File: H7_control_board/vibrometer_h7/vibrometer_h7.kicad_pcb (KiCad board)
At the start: 4 copper layers, 100 x 130 mm, 73 parts, among them J1 USB_C_Receptacle_USB2.0_16P, J2 PJ-3270, Q201 BSS138, Q202 BSS138, SW201 SW_Push, SW501 SW_Push, SW502 SW_Push, U1 STM32H723VGTx, U2 USBLC6-2SC6, U3 AMS1117-3V3, U4 MT9700, U6 TPA6111A2

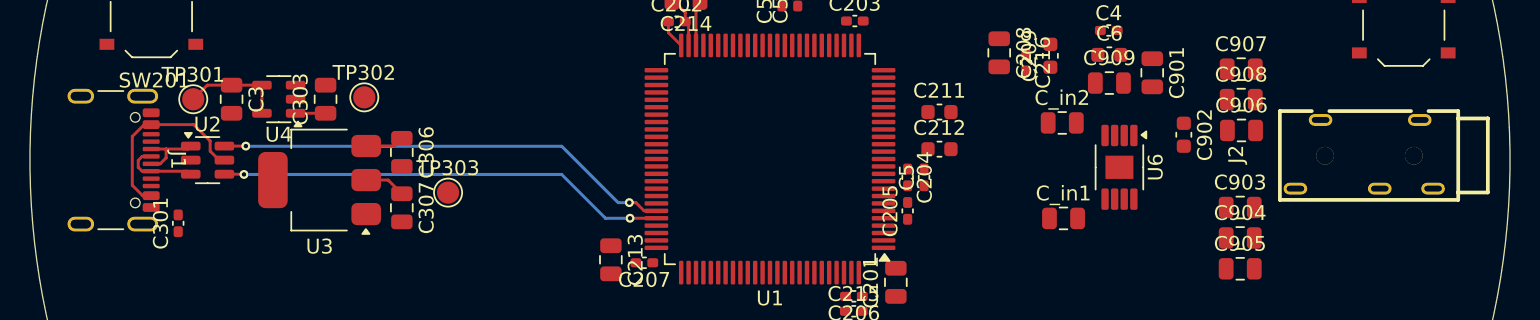
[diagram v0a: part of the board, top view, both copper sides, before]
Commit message: part selection for audio, schematic cleanup
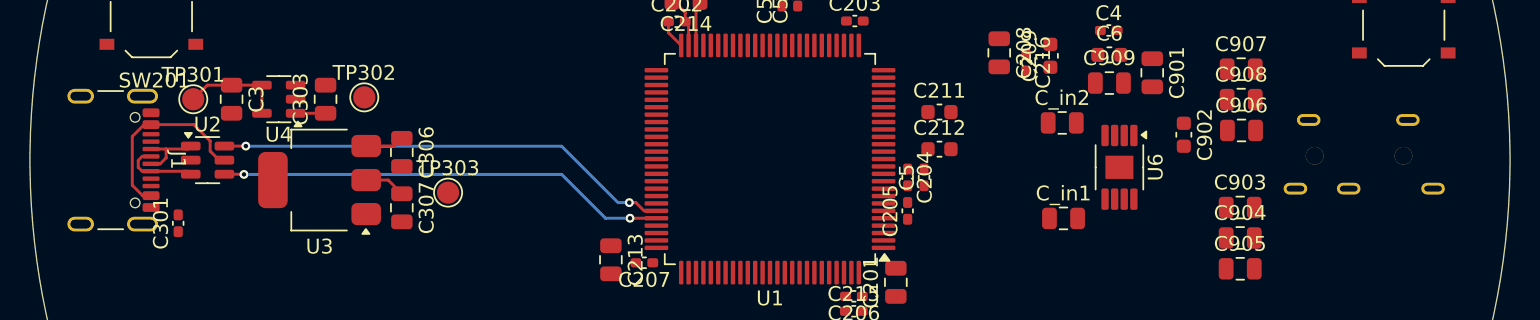
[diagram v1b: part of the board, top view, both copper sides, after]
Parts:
- J2: moved to B.Cu

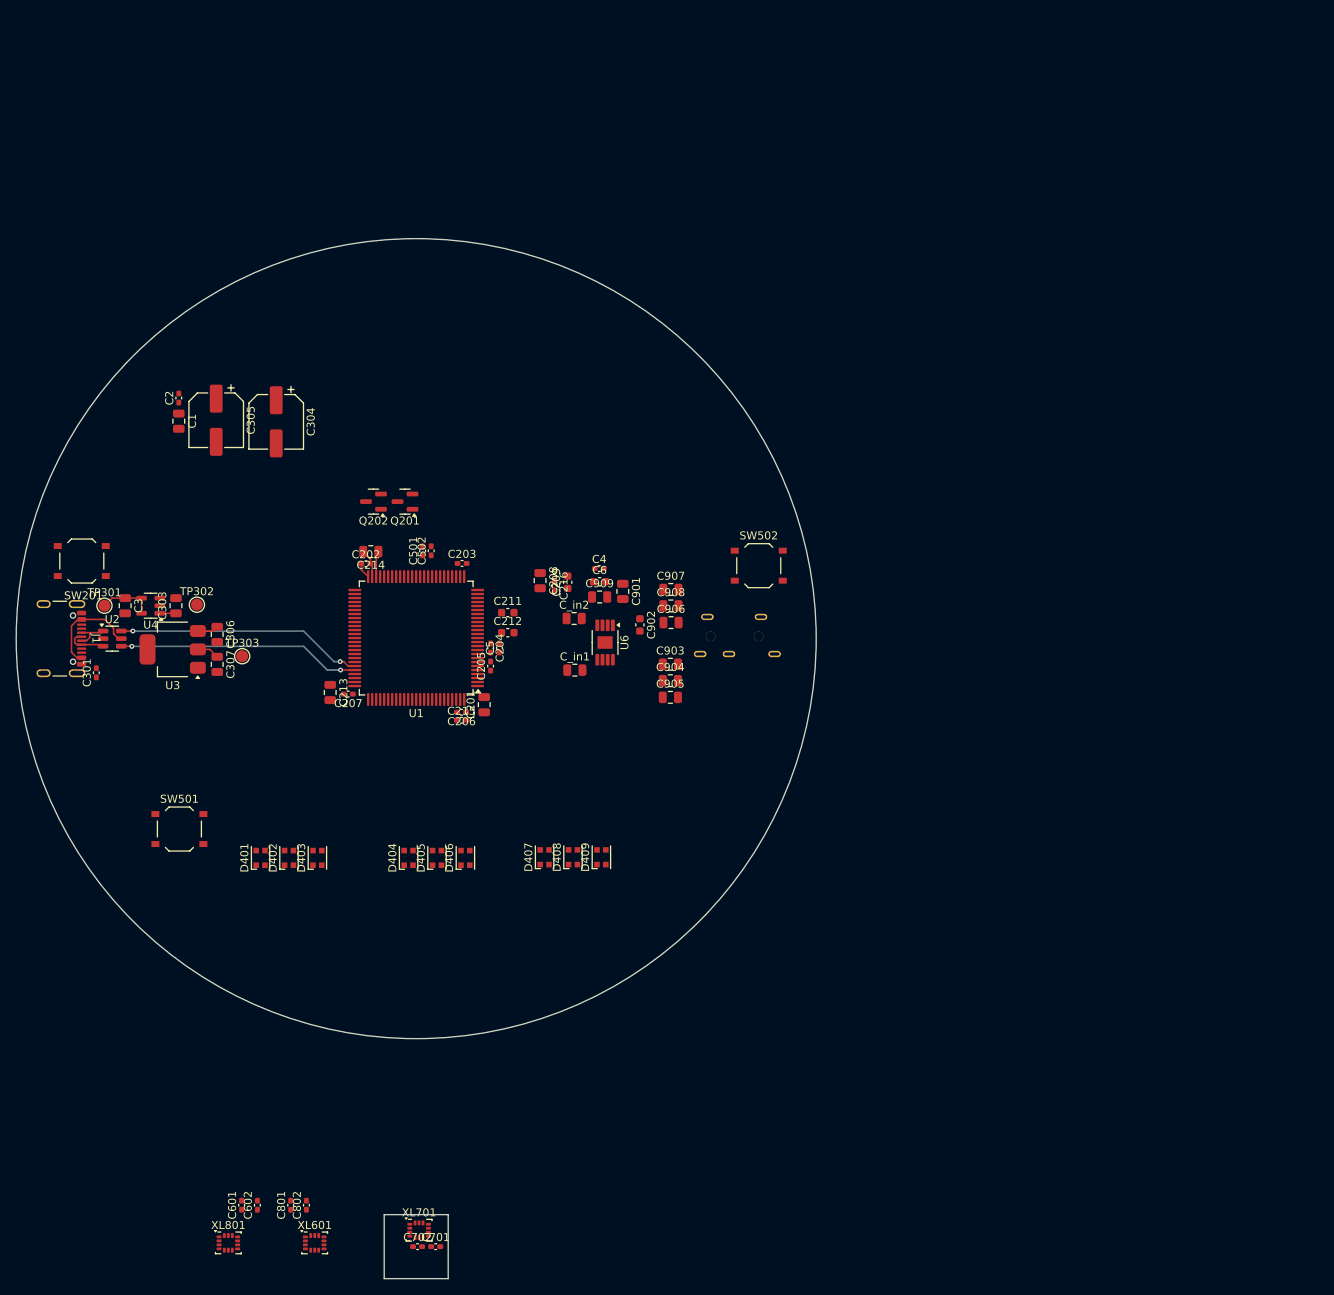
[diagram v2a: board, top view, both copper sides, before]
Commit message: first pass at board routing
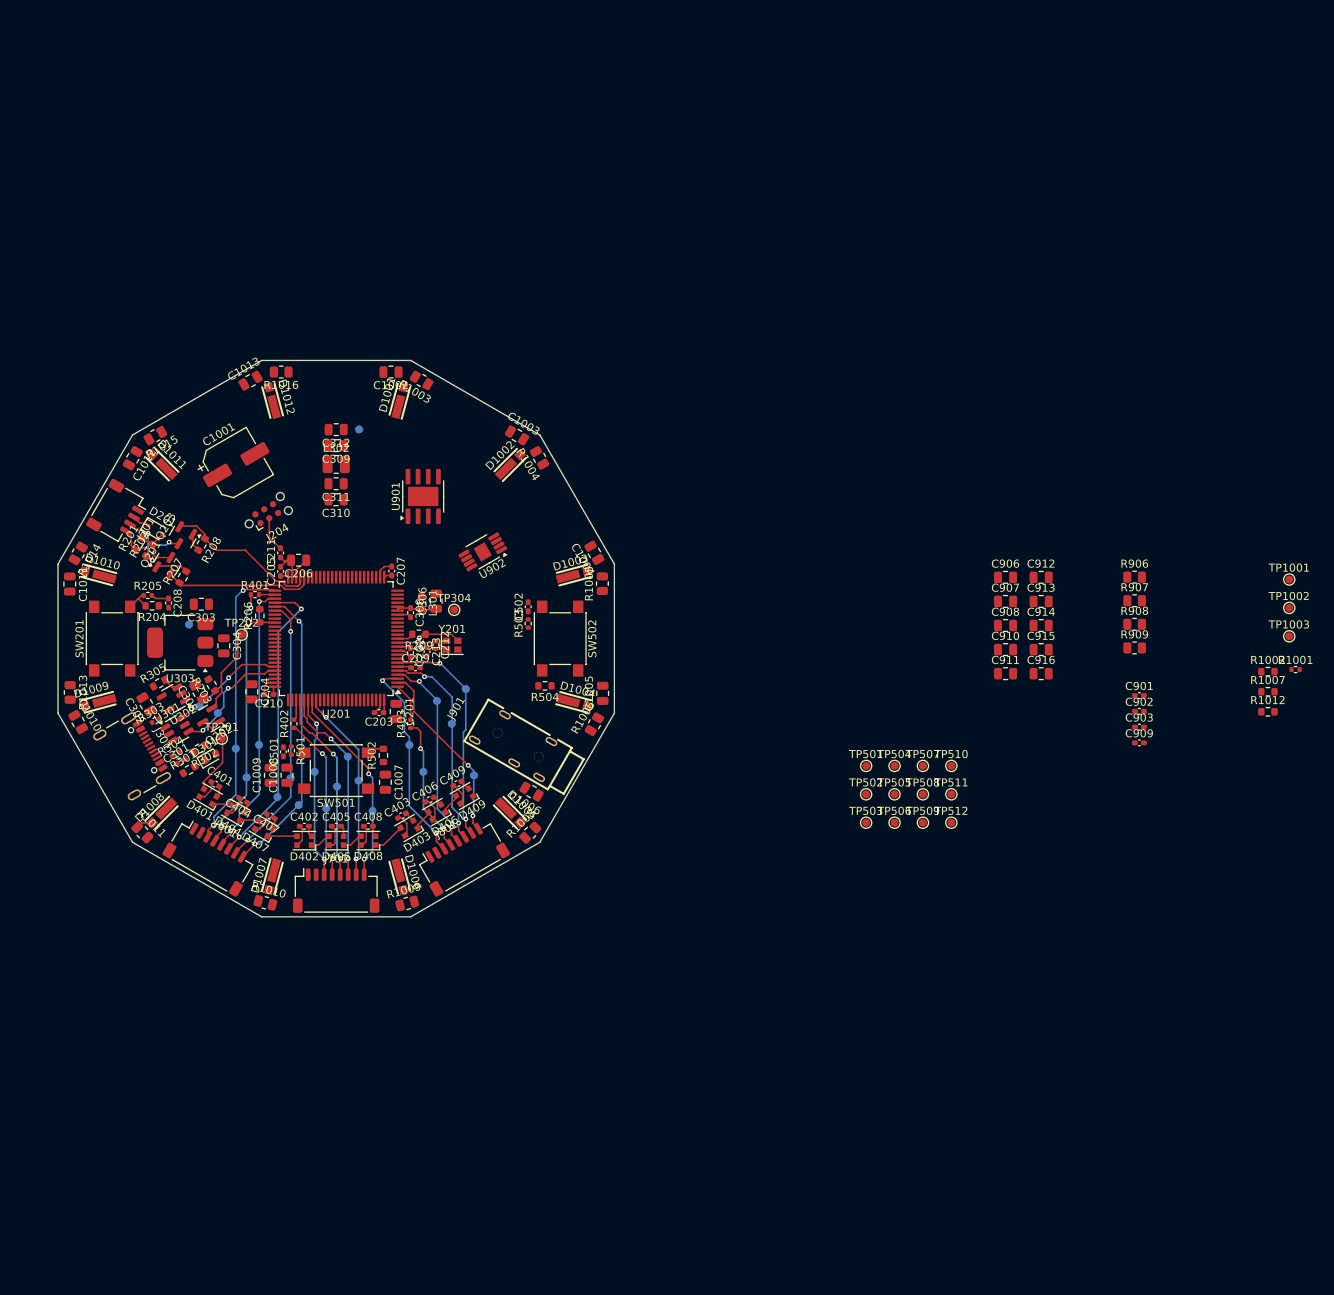
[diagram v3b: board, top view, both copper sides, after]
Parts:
- removed C1, C3: 10u, Capacitor_SMD:C_0805_2012Metric
- removed C2, C215, C216, C4, C5, C601, C602, C701, C702, C801, C802: 100n, Capacitor_SMD:C_0402_1005Metric_Pad0.74x0.62mm_HandSolder
- removed C214, C_in1, C_in2: 2u2, Capacitor_SMD:C_0805_2012Metric
- removed C307, C904, C905: 22u, Capacitor_SMD:C_0805_2012Metric
- removed C6: C_Small, Capacitor_SMD:C_0603_1608Metric
- removed J1: USB_C_Receptacle_USB2.0_16P, Connector_USB:USB_C_Receptacle_GCT_USB4105-xx-A_16P_TopMnt_Horizontal
- removed J2: PJ-3270, footprints:AUDIO-TH_PJ-3270
- removed TP301: TP_V_USB, TestPoint:TestPoint_Pad_D1.5mm
- removed TP303: TP_3V3, TestPoint:TestPoint_Pad_D1.5mm
- removed U1: STM32H723VGTx, Package_QFP:LQFP-100_14x14mm_P0.5mm
- removed U2: USBLC6-2SC6, Package_TO_SOT_SMD:SOT-23-6
- removed U3: AMS1117-3V3, Package_TO_SOT_SMD:SOT-223-3_TabPin2
- removed U4: MT9700, Package_TO_SOT_SMD:SOT-23-5
- removed U6: TPA6111A2, Package_SO:HVSSOP-8-1EP_3x3mm_P0.65mm_EP1.57x1.89mm
- removed XL601, XL701, XL801: LSM6DS3, Package_LGA:LGA-14_3x2.5mm_P0.5mm_LayoutBorder3x4y
- added C1001: 150u, Capacitor_SMD:CP_Elec_6.3x7.7, F.Cu at (137.5, 78.2)
- added C1002: 10u, Capacitor_SMD:C_0805_2012Metric, F.Cu at (156.8, 66.7)
- added C1003: 10u, Capacitor_SMD:C_0805_2012Metric, F.Cu at (172.6, 74.6)
- added C1004: 10u, Capacitor_SMD:C_0805_2012Metric, F.Cu at (182.3, 89.3)
- added C1005: 10u, Capacitor_SMD:C_0805_2012Metric, F.Cu at (183.3, 106.8)
- added C1006: 10u, Capacitor_SMD:C_0805_2012Metric, F.Cu at (174.4, 119.1)
- added C1007: 10u, Capacitor_SMD:C_0805_2012Metric, F.Cu at (156.2, 118.0)
- added C1008: 10u, Capacitor_SMD:C_0805_2012Metric, F.Cu at (143.8, 117.1)
- added C1009: 10u, Capacitor_SMD:C_0805_2012Metric, F.Cu at (141.8, 117.1)
- added C1010: 10u, Capacitor_SMD:C_0805_2012Metric, F.Cu at (117.8, 110.4)
- added C1011: 10u, Capacitor_SMD:C_0805_2012Metric, F.Cu at (116.7, 93.2)
- added C1012: 10u, Capacitor_SMD:C_0805_2012Metric, F.Cu at (124.6, 77.5)
- added C1013: 10u, Capacitor_SMD:C_0805_2012Metric, F.Cu at (139.3, 67.8)
- added C210: 100n, Capacitor_SMD:C_0402_1005Metric_Pad0.74x0.62mm_HandSolder, F.Cu at (141.6, 107.0)
- added C302: 10u, Capacitor_SMD:C_0805_2012Metric, F.Cu at (126.3, 108.2)
- added C308: 100n, Capacitor_SMD:C_0402_1005Metric_Pad0.74x0.62mm_HandSolder, F.Cu at (159.3, 96.8)
- added C309: 22u, Capacitor_SMD:C_0805_2012Metric, F.Cu at (150.0, 75.9)
- added C310: 22u, Capacitor_SMD:C_0805_2012Metric, F.Cu at (150.0, 82.6)
- added C311: 22u, Capacitor_SMD:C_0805_2012Metric, F.Cu at (150.0, 80.6)
- added C312: 22u, Capacitor_SMD:C_0805_2012Metric, F.Cu at (150.0, 73.9)
- added C401: 100n, Capacitor_SMD:C_0402_1005Metric_Pad0.74x0.62mm_HandSolder, F.Cu at (134.9, 118.2)
- added C402: 100n, Capacitor_SMD:C_0402_1005Metric_Pad0.74x0.62mm_HandSolder, F.Cu at (146.0, 123.5)
- added C403: 100n, Capacitor_SMD:C_0402_1005Metric_Pad0.74x0.62mm_HandSolder, F.Cu at (158.2, 122.1)
- added C404: 100n, Capacitor_SMD:C_0402_1005Metric_Pad0.74x0.62mm_HandSolder, F.Cu at (138.3, 120.2)
- added C405: 100n, Capacitor_SMD:C_0402_1005Metric_Pad0.74x0.62mm_HandSolder, F.Cu at (150.0, 123.5)
- added C406: 100n, Capacitor_SMD:C_0402_1005Metric_Pad0.74x0.62mm_HandSolder, F.Cu at (161.7, 120.1)
- added C407: 100n, Capacitor_SMD:C_0402_1005Metric_Pad0.74x0.62mm_HandSolder, F.Cu at (141.8, 122.2)
- added C408: 100n, Capacitor_SMD:C_0402_1005Metric_Pad0.74x0.62mm_HandSolder, F.Cu at (154.0, 123.5)
- added C409: 100n, Capacitor_SMD:C_0402_1005Metric_Pad0.74x0.62mm_HandSolder, F.Cu at (165.1, 118.1)
- added C910: 1u, Capacitor_SMD:C_0805_2012Metric, F.Cu at (233.7, 101.4)
- added C911: 22u, Capacitor_SMD:C_0805_2012Metric, F.Cu at (233.7, 104.4)
- added C912: 22u, Capacitor_SMD:C_0805_2012Metric, F.Cu at (238.1, 92.3)
- added C913: 22u, Capacitor_SMD:C_0805_2012Metric, F.Cu at (238.1, 95.3)
- added C914: 22u, Capacitor_SMD:C_0805_2012Metric, F.Cu at (238.1, 98.4)
- added C915: 22u, Capacitor_SMD:C_0805_2012Metric, F.Cu at (238.1, 101.4)
- added C916: 22u, Capacitor_SMD:C_0805_2012Metric, F.Cu at (238.1, 104.4)
- added D1001: LED, footprints:LED-SMD_L4.0-W1.50_HL-A-4014H421W-S1-HR3-DM-HL, F.Cu at (158.1, 69.8)
- added D1002: LED, footprints:LED-SMD_L4.0-W1.50_HL-A-4014H421W-S1-HR3-DM-HL, F.Cu at (172.1, 77.9)
- added D1003: LED, footprints:LED-SMD_L4.0-W1.50_HL-A-4014H421W-S1-HR3-DM-HL, F.Cu at (180.2, 91.9)
- added D1004: LED, footprints:LED-SMD_L4.0-W1.50_HL-A-4014H421W-S1-HR3-DM-HL, F.Cu at (180.2, 108.1)
- added D1005: LED, footprints:LED-SMD_L4.0-W1.50_HL-A-4014H421W-S1-HR3-DM-HL, F.Cu at (172.1, 122.1)
- added D1006: LED, footprints:LED-SMD_L4.0-W1.50_HL-A-4014H421W-S1-HR3-DM-HL, F.Cu at (158.1, 130.2)
- added D1007: LED, footprints:LED-SMD_L4.0-W1.50_HL-A-4014H421W-S1-HR3-DM-HL, F.Cu at (141.9, 130.2)
- added D1008: LED, footprints:LED-SMD_L4.0-W1.50_HL-A-4014H421W-S1-HR3-DM-HL, F.Cu at (127.9, 122.1)
- added D1009: LED, footprints:LED-SMD_L4.0-W1.50_HL-A-4014H421W-S1-HR3-DM-HL, F.Cu at (119.8, 108.1)
- added D1010: LED, footprints:LED-SMD_L4.0-W1.50_HL-A-4014H421W-S1-HR3-DM-HL, F.Cu at (119.8, 91.9)
- added D1011: LED, footprints:LED-SMD_L4.0-W1.50_HL-A-4014H421W-S1-HR3-DM-HL, F.Cu at (127.9, 77.9)
- added D1012: LED, footprints:LED-SMD_L4.0-W1.50_HL-A-4014H421W-S1-HR3-DM-HL, F.Cu at (141.9, 69.8)
- added D201: Schottky Diode, Diode_SMD:D_SOD-323, F.Cu at (127.4, 86.4)
- added D301: LED, LED_SMD:LED_0603_1608Metric, F.Cu at (134.3, 114.8)
- added J201: Conn_01x04_Socket, Connector_JST:JST_SH_SM04B-SRSS-TB_1x04-1MP_P1.00mm_Horizontal, F.Cu at (122.8, 84.2)
- added J204: TC2030-NL, Connector:Tag-Connect_TC2030-IDC-NL_2x03_P1.27mm_Vertical, F.Cu at (141.3, 84.4)
- added J301: USB_C_Receptacle_USB2.0_16P, Connector_USB:USB_C_Receptacle_GCT_USB4105-xx-A_16P_TopMnt_Horizontal, F.Cu at (123.5, 115.2)
- added J601: Conn_01x08_Socket, Connector_JST:JST_SH_SM08B-SRSS-TB_1x08-1MP_P1.00mm_Horizontal, F.Cu at (134.2, 127.2)
- added J701: Conn_01x08_Socket, Connector_JST:JST_SH_SM08B-SRSS-TB_1x08-1MP_P1.00mm_Horizontal, F.Cu at (150.0, 131.5)
- added J801: Conn_01x08_Socket, Connector_JST:JST_SH_SM08B-SRSS-TB_1x08-1MP_P1.00mm_Horizontal, F.Cu at (165.8, 127.2)
- added J901: PJ-3270, footprints:AUDIO-TH_PJ-3270, F.Cu at (172.5, 113.0)
- added L301: 39n, Inductor_SMD:L_0603_1608Metric, F.Cu at (160.7, 95.5)
- added L302: 2u2, Inductor_SMD:L_1008_2520Metric, F.Cu at (150.0, 78.2)
- added Q203: BSS138, Package_TO_SOT_SMD:SOT-23, F.Cu at (130.8, 87.3)
- added R1001: 22, Resistor_SMD:R_0402_1005Metric, F.Cu at (269.9, 103.9)
- added R1002: 10k, Resistor_SMD:R_0603_1608Metric, F.Cu at (266.5, 104.1)
- added R1003: ??, Resistor_SMD:R_0805_2012Metric, F.Cu at (160.7, 67.7)
- added R1004: ??, Resistor_SMD:R_0805_2012Metric, F.Cu at (175.4, 77.4)
- added R1005: ??, Resistor_SMD:R_0805_2012Metric, F.Cu at (183.3, 93.1)
- added R1006: ??, Resistor_SMD:R_0805_2012Metric, F.Cu at (182.3, 110.7)
- added R1007: 10k, Resistor_SMD:R_0603_1608Metric, F.Cu at (266.5, 106.6)
- added R1008: ??, Resistor_SMD:R_0805_2012Metric, F.Cu at (174.3, 124.3)
- added R1009: ??, Resistor_SMD:R_0805_2012Metric, F.Cu at (158.9, 133.1)
- added R1010: ??, Resistor_SMD:R_0805_2012Metric, F.Cu at (141.2, 133.0)
- added R1011: ??, Resistor_SMD:R_0805_2012Metric, F.Cu at (125.8, 124.2)
- added R1012: 10k, Resistor_SMD:R_0603_1608Metric, F.Cu at (266.5, 109.2)
- added R1013: ??, Resistor_SMD:R_0805_2012Metric, F.Cu at (116.8, 106.7)
- added R1014: ??, Resistor_SMD:R_0805_2012Metric, F.Cu at (117.8, 89.3)
- added R1015: ??, Resistor_SMD:R_0805_2012Metric, F.Cu at (127.4, 74.6)
- added R1016: ??, Resistor_SMD:R_0805_2012Metric, F.Cu at (143.1, 66.7)
- added R201: 10k, Resistor_SMD:R_0603_1608Metric, F.Cu at (125.3, 88.2)
- added R202: 10k, Resistor_SMD:R_0603_1608Metric, F.Cu at (126.7, 89.0)
- added R203: 10k, Resistor_SMD:R_0603_1608Metric, F.Cu at (134.4, 105.8)
- added R204: 10k, Resistor_SMD:R_0603_1608Metric, F.Cu at (127.0, 95.9)
- added R205: 330, Resistor_SMD:R_0402_1005Metric, F.Cu at (126.5, 94.6)
- added R206: 10k, Resistor_SMD:R_0603_1608Metric, F.Cu at (140.4, 97.2)
- added R207: 10k, Resistor_SMD:R_0603_1608Metric, F.Cu at (130.8, 92.3)
- added R208: 10k, Resistor_SMD:R_0603_1608Metric, F.Cu at (133.2, 88.2)
- added R209: 47, Resistor_SMD:R_0603_1608Metric, F.Cu at (160.3, 99.5)
- added R301: 100k, Resistor_SMD:R_0603_1608Metric, F.Cu at (131.6, 116.4)
- added R302: 1k, Resistor_SMD:R_0603_1608Metric, F.Cu at (132.8, 113.8)
- added R303: 5K1, Resistor_SMD:R_0402_1005Metric, F.Cu at (127.4, 110.2)
- added R304: 5K1, Resistor_SMD:R_0402_1005Metric, F.Cu at (129.9, 114.5)
- added R305: 4k7, Resistor_SMD:R_0603_1608Metric, F.Cu at (127.9, 105.6)
- added R401: 22, Resistor_SMD:R_0402_1005Metric, F.Cu at (139.8, 94.5)
- added R402: 22, Resistor_SMD:R_0402_1005Metric, F.Cu at (144.7, 110.6)
- added R403: 22, Resistor_SMD:R_0402_1005Metric, F.Cu at (159.3, 110.7)
- added R501: 330, Resistor_SMD:R_0402_1005Metric, F.Cu at (144.4, 114.0)
- added R502: 10k, Resistor_SMD:R_0603_1608Metric, F.Cu at (155.9, 114.6)
- added R503: 330, Resistor_SMD:R_0402_1005Metric, F.Cu at (174.0, 98.1)
- added R504: 10k, Resistor_SMD:R_0603_1608Metric, F.Cu at (176.1, 105.9)
- added R906: 10k, Resistor_SMD:R_0805_2012Metric, F.Cu at (249.8, 92.3)
- added R907: 10k, Resistor_SMD:R_0805_2012Metric, F.Cu at (249.8, 95.3)
- added R908: 15k, Resistor_SMD:R_0805_2012Metric, F.Cu at (249.8, 98.2)
- added R909: 15k, Resistor_SMD:R_0805_2012Metric, F.Cu at (249.8, 101.2)
- added TP1001: TestPoint, TestPoint:TestPoint_Pad_D1.0mm, F.Cu at (269.1, 92.6)
- added TP1002: TestPoint, TestPoint:TestPoint_Pad_D1.0mm, F.Cu at (269.1, 96.2)
- added TP1003: TestPoint, TestPoint:TestPoint_Pad_D1.0mm, F.Cu at (269.1, 99.7)
- added TP11: TP_USB+, TestPoint:TestPoint_Pad_D1.0mm, B.Cu at (135.2, 109.3)
- added TP12: TP_USB-, TestPoint:TestPoint_Pad_D1.0mm, B.Cu at (132.9, 108.5)
- added TP201: RGBLED_5V, TestPoint:TestPoint_Pad_D1.0mm, F.Cu at (135.7, 112.5)
- added TP202: RGBLED_3V3, TestPoint:TestPoint_Pad_D1.0mm, F.Cu at (138.2, 99.5)
- added TP304: TP_3V3A, TestPoint:TestPoint_Pad_D1.0mm, F.Cu at (164.8, 96.4)
- added TP305: TP_5VA, TestPoint:TestPoint_Pad_D1.0mm, B.Cu at (152.9, 73.8)
- added TP401: TestPoint, TestPoint:TestPoint_Pad_D1.0mm, B.Cu at (145.3, 120.8)
- added TP402: TestPoint, TestPoint:TestPoint_Pad_D1.0mm, B.Cu at (144.3, 117.5)
- added TP403: TestPoint, TestPoint:TestPoint_Pad_D1.0mm, B.Cu at (140.3, 113.3)
- added TP404: TestPoint, TestPoint:TestPoint_Pad_D1.0mm, B.Cu at (142.7, 119.8)
- added TP405: TestPoint, TestPoint:TestPoint_Pad_D1.0mm, B.Cu at (138.8, 117.3)
- added TP406: TestPoint, TestPoint:TestPoint_Pad_D1.0mm, B.Cu at (137.4, 113.8)
- added TP407: TestPoint, TestPoint:TestPoint_Pad_D1.0mm, B.Cu at (154.6, 121.5)
- added TP408: TestPoint, TestPoint:TestPoint_Pad_D1.0mm, B.Cu at (152.8, 117.8)
- added TP409: TestPoint, TestPoint:TestPoint_Pad_D1.0mm, B.Cu at (150.1, 118.5)
- added TP410: TestPoint, TestPoint:TestPoint_Pad_D1.0mm, B.Cu at (151.4, 114.8)
- added TP411: TestPoint, TestPoint:TestPoint_Pad_D1.0mm, B.Cu at (148.8, 121.2)
- added TP412: TestPoint, TestPoint:TestPoint_Pad_D1.0mm, B.Cu at (147.3, 116.7)
- added TP413: TestPoint, TestPoint:TestPoint_Pad_D1.0mm, B.Cu at (167.2, 117.1)
- added TP414: TestPoint, TestPoint:TestPoint_Pad_D1.0mm, B.Cu at (166.2, 106.3)
- added TP415: TestPoint, TestPoint:TestPoint_Pad_D1.0mm, B.Cu at (162.6, 107.8)
- added TP416: TestPoint, TestPoint:TestPoint_Pad_D1.0mm, B.Cu at (164.4, 110.7)
- added TP417: TestPoint, TestPoint:TestPoint_Pad_D1.0mm, B.Cu at (160.9, 116.7)
- added TP418: TestPoint, TestPoint:TestPoint_Pad_D1.0mm, B.Cu at (159.2, 113.3)
- added TP501: TestPoint, TestPoint:TestPoint_Pad_D1.0mm, F.Cu at (216.2, 115.9)
- added TP502: TestPoint, TestPoint:TestPoint_Pad_D1.0mm, F.Cu at (216.2, 119.5)
- added TP503: TestPoint, TestPoint:TestPoint_Pad_D1.0mm, F.Cu at (216.2, 123.0)
- added TP504: TestPoint, TestPoint:TestPoint_Pad_D1.0mm, F.Cu at (219.8, 115.9)
- added TP505: TestPoint, TestPoint:TestPoint_Pad_D1.0mm, F.Cu at (219.8, 119.5)
- added TP506: TestPoint, TestPoint:TestPoint_Pad_D1.0mm, F.Cu at (219.8, 123.0)
- added TP507: TestPoint, TestPoint:TestPoint_Pad_D1.0mm, F.Cu at (223.3, 115.9)
- added TP508: TestPoint, TestPoint:TestPoint_Pad_D1.0mm, F.Cu at (223.3, 119.5)
- added TP509: TestPoint, TestPoint:TestPoint_Pad_D1.0mm, F.Cu at (223.3, 123.0)
- added TP510: TestPoint, TestPoint:TestPoint_Pad_D1.0mm, F.Cu at (226.9, 115.9)
- added TP511: TestPoint, TestPoint:TestPoint_Pad_D1.0mm, F.Cu at (226.9, 119.5)
- added TP512: TestPoint, TestPoint:TestPoint_Pad_D1.0mm, F.Cu at (226.9, 123.0)
- added U201: STM32H723VGTx, Package_QFP:LQFP-100_14x14mm_P0.5mm, F.Cu at (150.0, 100.0)
- added U301: USBLC6-2SC6, Package_TO_SOT_SMD:SOT-23-6, F.Cu at (130.1, 111.3)
- added U302: MT9700, Package_TO_SOT_SMD:SOT-23-5, F.Cu at (129.7, 107.5)
- added U303: AMS1117-3V3, Package_TO_SOT_SMD:SOT-223-3_TabPin2, F.Cu at (130.5, 100.5)
- added U901: RC4580, Package_SO:SOIC-8-1EP_3.9x4.9mm_P1.27mm_EP2.41x3.81mm, F.Cu at (160.9, 82.2)
- added U902: TPA6111A2, Package_SO:HVSSOP-8-1EP_3x3mm_P0.65mm_EP1.57x1.89mm, F.Cu at (168.3, 89.2)
- added Y201: 24MHz, Crystal:Crystal_SMD_2016-4Pin_2.0x1.6mm, F.Cu at (164.5, 100.8)
- C204, C206: value 100n -> 2u2; footprint Capacitor_SMD:C_0402_1005Metric_Pad0.74x0.62mm_HandSolder -> Capacitor_SMD:C_0805_2012Metric
- C208, C901: value 1u -> 100n; footprint Capacitor_SMD:C_0805_2012Metric -> Capacitor_SMD:C_0402_1005Metric_Pad0.74x0.62mm_HandSolder
- C209: value 10n -> 100n; footprint Capacitor_SMD:C_0603_1608Metric -> Capacitor_SMD:C_0402_1005Metric_Pad0.74x0.62mm_HandSolder
- C211: value 12p -> 100n; footprint Capacitor_SMD:C_0603_1608Metric -> Capacitor_SMD:C_0402_1005Metric_Pad0.74x0.62mm_HandSolder
- C212: footprint Capacitor_SMD:C_0603_1608Metric -> Capacitor_SMD:C_0402_1005Metric
- C213: value 2u2 -> 12p; footprint Capacitor_SMD:C_0805_2012Metric -> Capacitor_SMD:C_0402_1005Metric
- C304: value 150u -> 22u; footprint Capacitor_SMD:CP_Elec_6.3x7.7 -> Capacitor_SMD:C_0805_2012Metric
- C305: value 150u -> 10u; footprint Capacitor_SMD:CP_Elec_6.3x7.7 -> Capacitor_SMD:C_0805_2012Metric
- C306: value 10u -> 1u
- C902: footprint Capacitor_SMD:C_0603_1608Metric -> Capacitor_SMD:C_0402_1005Metric_Pad0.74x0.62mm_HandSolder
- C903: value 22u -> 100n; footprint Capacitor_SMD:C_0805_2012Metric -> Capacitor_SMD:C_0402_1005Metric_Pad0.74x0.62mm_HandSolder
- C906, C907: value 22u -> 2u2
- C908: value 22u -> 10u
- C909: value 10u -> 100n; footprint Capacitor_SMD:C_0805_2012Metric -> Capacitor_SMD:C_0402_1005Metric_Pad0.74x0.62mm_HandSolder
- SW201, SW501, SW502: footprint Button_Switch_SMD:SW_Push_1P1T_XKB_TS-1187A -> Button_Switch_SMD:SW_SPST_PTS645
- TP302: footprint TestPoint:TestPoint_Pad_D1.5mm -> TestPoint:TestPoint_Pad_D1.0mm; moved to B.Cu
- moved C909 69.9 mm to (250.4, 113.0)
- moved C901 65.9 mm to (250.4, 107.1), turned to 0 degrees
- moved C902 63.4 mm to (250.4, 109.1), turned to 0 degrees
- moved C903 59.2 mm to (250.4, 111.1)
- moved C208 46.5 mm to (129.1, 95.5)
- moved C906 42.2 mm to (233.7, 92.3)
- moved C908 41.9 mm to (233.7, 98.4)
- moved C907 41.9 mm to (233.7, 95.3)
- moved D407 35.3 mm to (140.9, 123.8), turned to 150 degrees
- moved C305 34.0 mm to (132.9, 106.7), turned to 120 degrees
- moved Q202 34.0 mm to (134.1, 110.0), turned to -150 degrees
- moved Q201 30.7 mm to (128.9, 90.7), turned to 60 degrees
- moved C501 30.6 mm to (143.4, 114.2)
- moved C204 30.3 mm to (139.4, 106.7)
- moved C211 29.4 mm to (143.1, 89.3), turned to 90 degrees
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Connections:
- C204 pad 1: +3V3 -> /MCU/VCAP2
- C206 pad 1: +3V3 -> /MCU/VCAP1
- C208 pad 1: +3V3A -> /MCU/BOOT0
- C209 pad 1: +3V3A -> +3V3
- C211 pad 1: /MCU/HSE_IN -> GND
- C211 pad 2: GND -> /MCU/SWD_NRST
- C212 pad 1: Net-(C212-Pad1) -> /MCU/HSE_IN
- C213 pad 1: /MCU/VCAP2 -> Net-(C213-Pad1)
- C304 pad 1: +5V -> +3V3
- C306 pad 1: +5V -> +3V3A
- C901 pad 2: Net-(U6-BYPASS) -> +5V
- C902 pad 1: +3V3A -> GND
- C902 pad 2: GND -> Net-(U901A-+)
- C903 pad 1: Net-(U6-VO1) -> GND
- C906 pad 1: Net-(U6-VO2) -> Net-(C904-Pad1)
- C907 pad 1: Net-(U6-VO2) -> Net-(C905-Pad1)
- C907 pad 2: Net-(C906-Pad2) -> Net-(C907-Pad2)
- C908 pad 1: Net-(U6-VO2) -> +5V
- C908 pad 2: Net-(C906-Pad2) -> GND
- C909 pad 1: +3V3A -> +5V
- D402 pad 3: Net-(D401-DOUT) -> Net-(D402-DIN)
- D403 pad 3: Net-(D402-DOUT) -> Net-(D403-DIN)
- D404 pad 3: Net-(D403-DOUT) -> Net-(D401-DOUT)
- D405 pad 3: Net-(D404-DOUT) -> Net-(D402-DOUT)
- D406 pad 3: Net-(D405-DOUT) -> Net-(D403-DOUT)
- D407 pad 1: Net-(D407-DOUT) -> Net-(D402-DIN)
- D407 pad 3: Net-(D406-DOUT) -> Net-(D404-DOUT)
- D408 pad 1: Net-(D408-DOUT) -> Net-(D403-DIN)
- D408 pad 3: Net-(D407-DOUT) -> Net-(D405-DOUT)
- D409 pad 3: Net-(D408-DOUT) -> Net-(D406-DOUT)
- Q201 pad 2: /MCU/SCL_QT -> /MCU/I2C2_SCL
- Q201 pad 3: /MCU/I2C2_SCL -> /MCU/SCL_QT
- Q202 pad 2: /MCU/STA_QT -> /MCU/LED_ACCEL_3V3
- Q202 pad 3: /MCU/I2C2_SDA -> /ACCEL/LED_ACCEL
- SW502 pad 2: /UI/BIG_RED_SW -> /UI/MUTE_SW
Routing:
- net /ACCEL/ACCEL.MOSI1: track 0.00 -> 37.4 mm, vias 0 -> 2
- net /ACCEL/ACCEL.INTA1: track 0.00 -> 36.8 mm, vias 0 -> 2
- net /ACCEL/ACCEL.NCS1: track 0.00 -> 36.7 mm, vias 0 -> 2
- net /ACCEL/ACCEL.MISO1: track 0.00 -> 34.4 mm, vias 0 -> 2
- net /ACCEL/ACCEL.INTB1: track 0.00 -> 34.4 mm, vias 0 -> 2
- net /ACCEL/SPI ACCELEROMETER1/ACCEL_SCK: track 0.00 -> 32.6 mm, vias 0 -> 2
- net /ACCEL/ACCEL.INTB3: track 0.00 -> 28.4 mm, vias 0 -> 2
- net /ACCEL/ACCEL.MOSI3: track 0.00 -> 26.3 mm, vias 0 -> 2
- net /ACCEL/ACCEL.NCS3: track 0.00 -> 26.2 mm, vias 0 -> 2
- net /ACCEL/ACCEL.INTA2: track 0.00 -> 25.4 mm, vias 0 -> 2
- net /ACCEL/ACCEL.MISO3: track 0.00 -> 25.0 mm, vias 0 -> 2
- net /ACCEL/ACCEL.MOSI2: track 0.00 -> 24.6 mm, vias 0 -> 2
- net +5V: track 4.65 -> 29.3 mm
- net /ACCEL/ACCEL.INTB2: track 0.00 -> 24.2 mm, vias 0 -> 2
- net /ACCEL/ACCEL.MISO2: track 0.00 -> 24.1 mm, vias 0 -> 2
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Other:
- board size 100 x 130 mm -> 69.5 x 69.5 mm

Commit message: lots of routing progress!!
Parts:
- removed R1001: 22, Resistor_SMD:R_0402_1005Metric
- removed TP202: RGBLED_3V3, TestPoint:TestPoint_Pad_D1.0mm
- added J202: Conn_02x06, Connector_PinHeader_1.00mm:PinHeader_2x06_P1.00mm_Vertical_SMD, F.Cu at (150.0, 70.5)
- added J501: Conn_02x08_Odd_Even, Connector_PinHeader_1.00mm:PinHeader_2x08_P1.00mm_Vertical_SMD, F.Cu at (164.6, 74.7)
- added J502: Conn_02x08_Odd_Even, Connector_PinHeader_1.00mm:PinHeader_2x08_P1.00mm_Vertical_SMD, F.Cu at (175.3, 85.4)
- added TP513: TestPoint, TestPoint:TestPoint_Pad_D1.0mm, B.Cu at (172.1, 86.6)
- added TP514: TestPoint, TestPoint:TestPoint_Pad_D1.0mm, B.Cu at (174.1, 84.4)
- added TP515: TestPoint, TestPoint:TestPoint_Pad_D1.0mm, B.Cu at (171.0, 84.9)
- added TP516: TestPoint, TestPoint:TestPoint_Pad_D1.0mm, B.Cu at (172.9, 82.7)
- TP1001, TP1002, TP1003, TP304, TP501, TP502, TP503, TP504, TP505, TP506, TP507, TP508, TP509, TP510, TP511, TP512: moved to B.Cu
- moved R1012 135.6 mm to (133.3, 83.4), turned to -90 degrees
- moved R1002 133.3 mm to (134.8, 83.4), turned to -90 degrees
- moved R1007 132.2 mm to (136.3, 83.4), turned to -90 degrees
- moved TP1003 128.9 mm to (140.4, 92.3), turned to 180 degrees
- moved TP1001 126.7 mm to (142.5, 97.8), turned to 180 degrees
- moved TP1002 126.2 mm to (142.9, 95.5), turned to 180 degrees
- moved TP508 77.2 mm to (161.2, 73.6), turned to 180 degrees
- moved TP506 74.6 mm to (163.0, 74.6), turned to 180 degrees
- moved TP507 74.1 mm to (160.7, 76.3), turned to 180 degrees
- moved C901 74.1 mm to (190.9, 62.9)
- moved C902 74.1 mm to (190.9, 64.9)
- moved C903 74.1 mm to (190.9, 66.8)
- moved C909 74.1 mm to (190.9, 68.8)
- moved R908 72.8 mm to (185.2, 58.9)
- moved R909 72.8 mm to (185.2, 61.8)
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- renumbered C404 to C402, C407 to C403, C402 to C404, C408 to C406, C403 to C407, C406 to C408, D404 to D402, D407 to D403, D402 to D404, D408 to D406, D403 to D407, D406 to D408, R906 to R908, R907 to R909, R908 to R910, R909 to R911, TP405 to TP401, TP411 to TP402, TP417 to TP403, TP401 to TP404, TP402 to TP405, TP403 to TP406, TP404 to TP407, TP406 to TP408, TP407 to TP409, TP408 to TP410, TP409 to TP411, TP410 to TP412, TP412 to TP413, TP413 to TP414, TP414 to TP415, TP415 to TP416, TP416 to TP417
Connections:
- net Net-(C904-Pad1) renamed /AUDIO/AMP1_OUT
- net Net-(C905-Pad1) renamed /AUDIO/AMP2_OUT
- net Net-(C911-Pad2) renamed /AUDIO/AUDIO_R
- net Net-(C914-Pad2) renamed /AUDIO/AUDIO_L
- net Net-(D201-K) renamed /MCU/5V_QT
- net Net-(U901A-+) renamed /AUDIO/AMP1_IN
- net Net-(U901A--) renamed /AUDIO/AMP1_FB
- net Net-(U901B-+) renamed /AUDIO/AMP2_IN
- net Net-(U901B--) renamed /AUDIO/AMP2_FB
- net Net-(U902-BYPASS) renamed /AUDIO/LN_BYPASS
- net Net-(U902-IN1-) renamed /AUDIO/LN_IN1
- net Net-(U902-IN2-) renamed /AUDIO/LN_IN2
- net Net-(U902-VO1) renamed /AUDIO/LN_OUT1
- net Net-(U902-VO2) renamed /AUDIO/LN_OUT2
- C901 pad 2: +5V -> +5VA
- C908 pad 1: +5V -> +5VA
- C909 pad 1: +5V -> +5VA
- D1001 pad 1: Net-(D1001-K) -> /STROBE/FET1_D
- D1002 pad 1: Net-(D1001-K) -> /STROBE/FET2_D
- D1003 pad 1: Net-(D1001-K) -> /STROBE/FET3_D
- D1004 pad 1: Net-(D1001-K) -> /STROBE/FET1_D
- D1005 pad 1: Net-(D1005-K) -> /STROBE/FET2_D
- D1006 pad 1: Net-(D1005-K) -> /STROBE/FET3_D
- D1007 pad 1: Net-(D1005-K) -> /STROBE/FET1_D
- D1008 pad 1: Net-(D1005-K) -> /STROBE/FET2_D
- D1009 pad 1: Net-(D1009-K) -> /STROBE/FET3_D
- D1010 pad 1: Net-(D1009-K) -> /STROBE/FET1_D
- D1011 pad 1: Net-(D1009-K) -> /STROBE/FET2_D
- D1012 pad 1: Net-(D1009-K) -> /STROBE/FET3_D
- R1002 pad 2: Net-(Q1001-G) -> /MCU/LED_STROBE_1
- TP1001 pad 1: Net-(Q1001-G) -> /MCU/LED_STROBE_1
- U201 pad 24: unconnected-(U201-PA2-Pad24) -> /MCU/MUTE_BUTTON
- U201 pad 25: unconnected-(U201-PA3-Pad25) -> /AUDIO/MUTE_SIGNAL
- U201 pad 30: /AUDIO/MUTE_SIGNAL -> /MCU/ADC2_INP
- U201 pad 31: unconnected-(U201-PA7-Pad31) -> /MCU/ADC2_INN
- U201 pad 32: unconnected-(U201-PC4-Pad32) -> /MCU/ADC1_INP
- U201 pad 33: unconnected-(U201-PC5-Pad33) -> /MCU/ADC1_INN
- U201 pad 35: /MCU/MUTE_BUTTON -> unconnected-(U201-PB1-Pad35)
- U201 pad 36: /MCU/BIG_RED_BUTTON -> unconnected-(U201-PB2-Pad36)
- U201 pad 37: unconnected-(U201-PE7-Pad37) -> /MCU/UART_RX
- U201 pad 38: unconnected-(U201-PE8-Pad38) -> /MCU/UART_TX
- U201 pad 39: /MCU/DAC_EXT_TRG -> /MCU/UART_RTS
- U201 pad 40: unconnected-(U201-PE10-Pad40) -> /MCU/UART_CTS
- U201 pad 66: unconnected-(U201-PC9-Pad66) -> /MCU/DAC_EXT_TRG
- U201 pad 77: unconnected-(U201-PA15(JTDI)-Pad77) -> /MCU/BIG_RED_BUTTON
- U901 pad 8: +5V -> +5VA
- U902 pad 6: +5V -> +5VA
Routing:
- net +3V3: track 15.8 -> 255.4 mm, vias 0 -> 22
- net /STROBE/FET2_D: track 0.00 -> 177.1 mm, vias 0 -> 4
- net /STROBE/FET1_D: track 0.00 -> 172.2 mm, vias 0 -> 4
- net /STROBE/FET3_D: track 0.00 -> 167.6 mm, vias 0 -> 4
- net +5V: track 29.3 -> 184.6 mm, vias 0 -> 19
- net GND: track 25.9 -> 119.9 mm, vias 0 -> 61
- net /MCU/VCP_RX: track 0.00 -> 41.3 mm, vias 0 -> 4
- net /MCU/VCP_TX: track 0.00 -> 40.9 mm, vias 0 -> 4
- net /MCU/SWD_CLK: track 0.00 -> 39.0 mm, vias 0 -> 2
- net /MCU/BOOT0: track 2.16 -> 35.1 mm, vias 0 -> 4
- net /MCU/SWD_SWO: track 0.00 -> 32.4 mm, vias 0 -> 2
- net /MCU/SWD_DIO: track 0.00 -> 27.0 mm, vias 0 -> 2
- net /MCU/ADC1_INN: track 0.00 -> 24.7 mm, vias 0 -> 2
- net /MCU/ADC1_INP: track 0.00 -> 24.5 mm, vias 0 -> 2
- net /MCU/ADC2_INN: track 0.00 -> 24.5 mm, vias 0 -> 2
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- added copper zone on In2.Cu, net +5V
- added copper zone on In1.Cu, net GND
- added copper zone on In2.Cu, net GND
